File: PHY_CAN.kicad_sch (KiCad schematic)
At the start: 6 parts, among them U3 SN65HVD230, U4 SN65HVD230

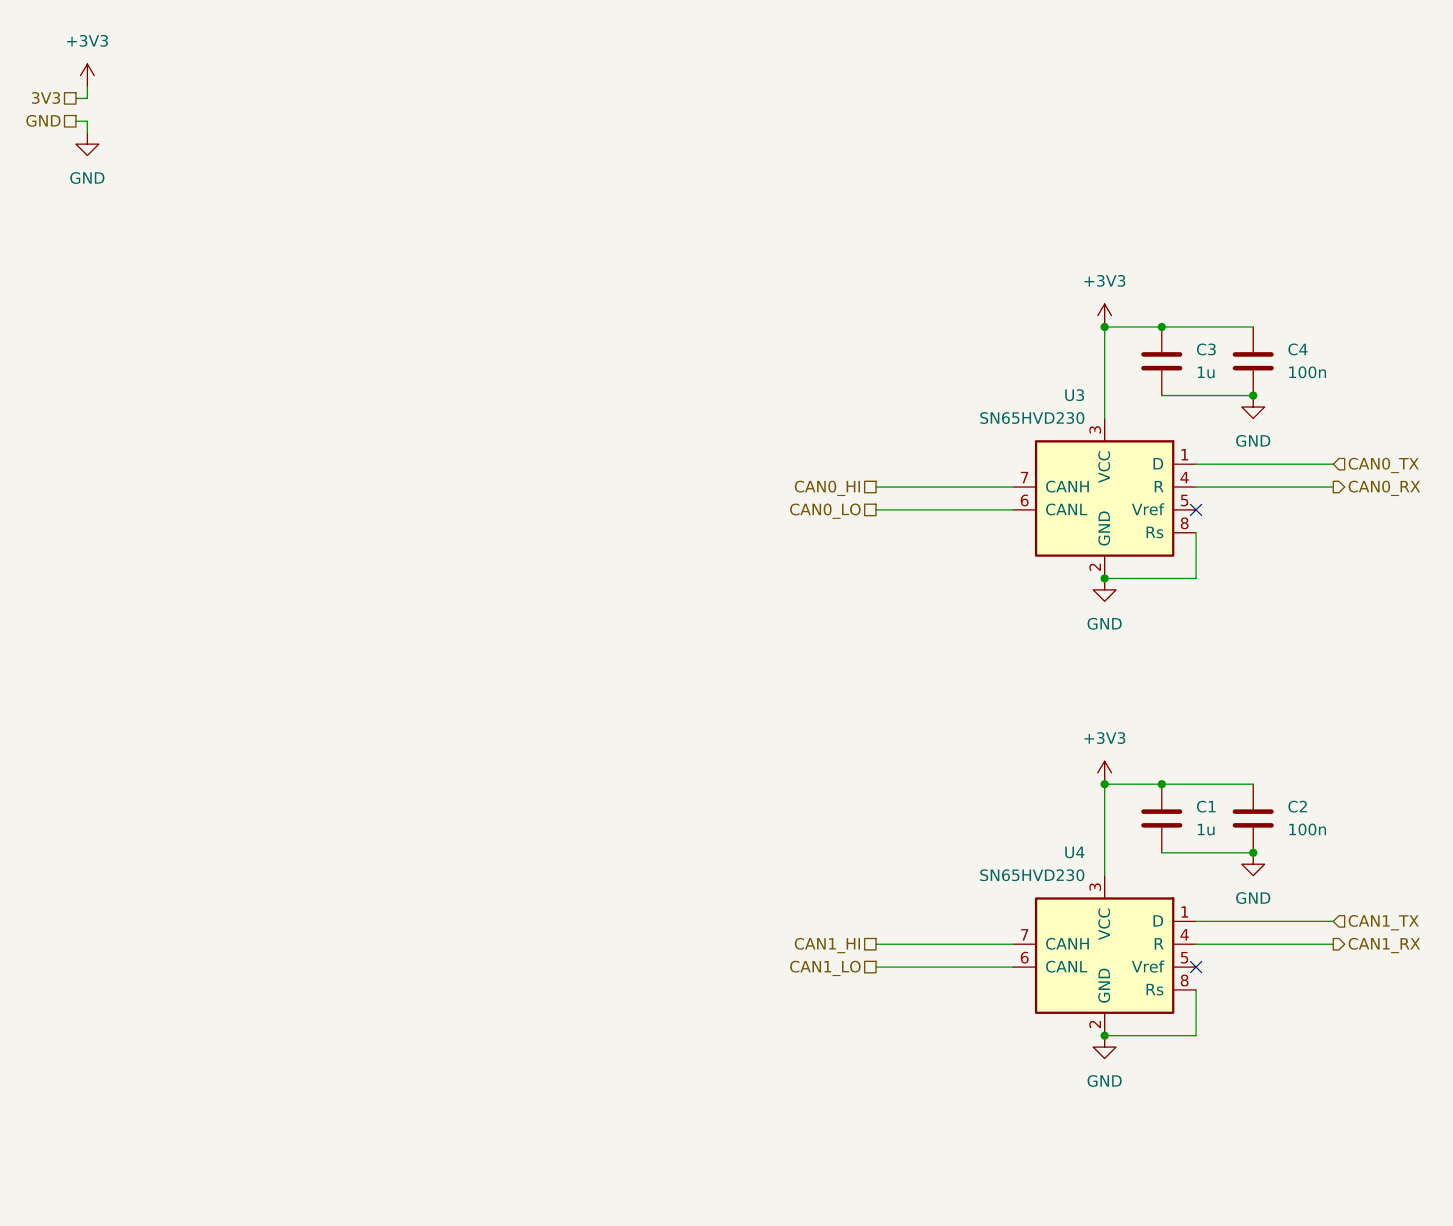
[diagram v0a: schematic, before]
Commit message: routed more sheets, improved analogs. next 5v /analog ground
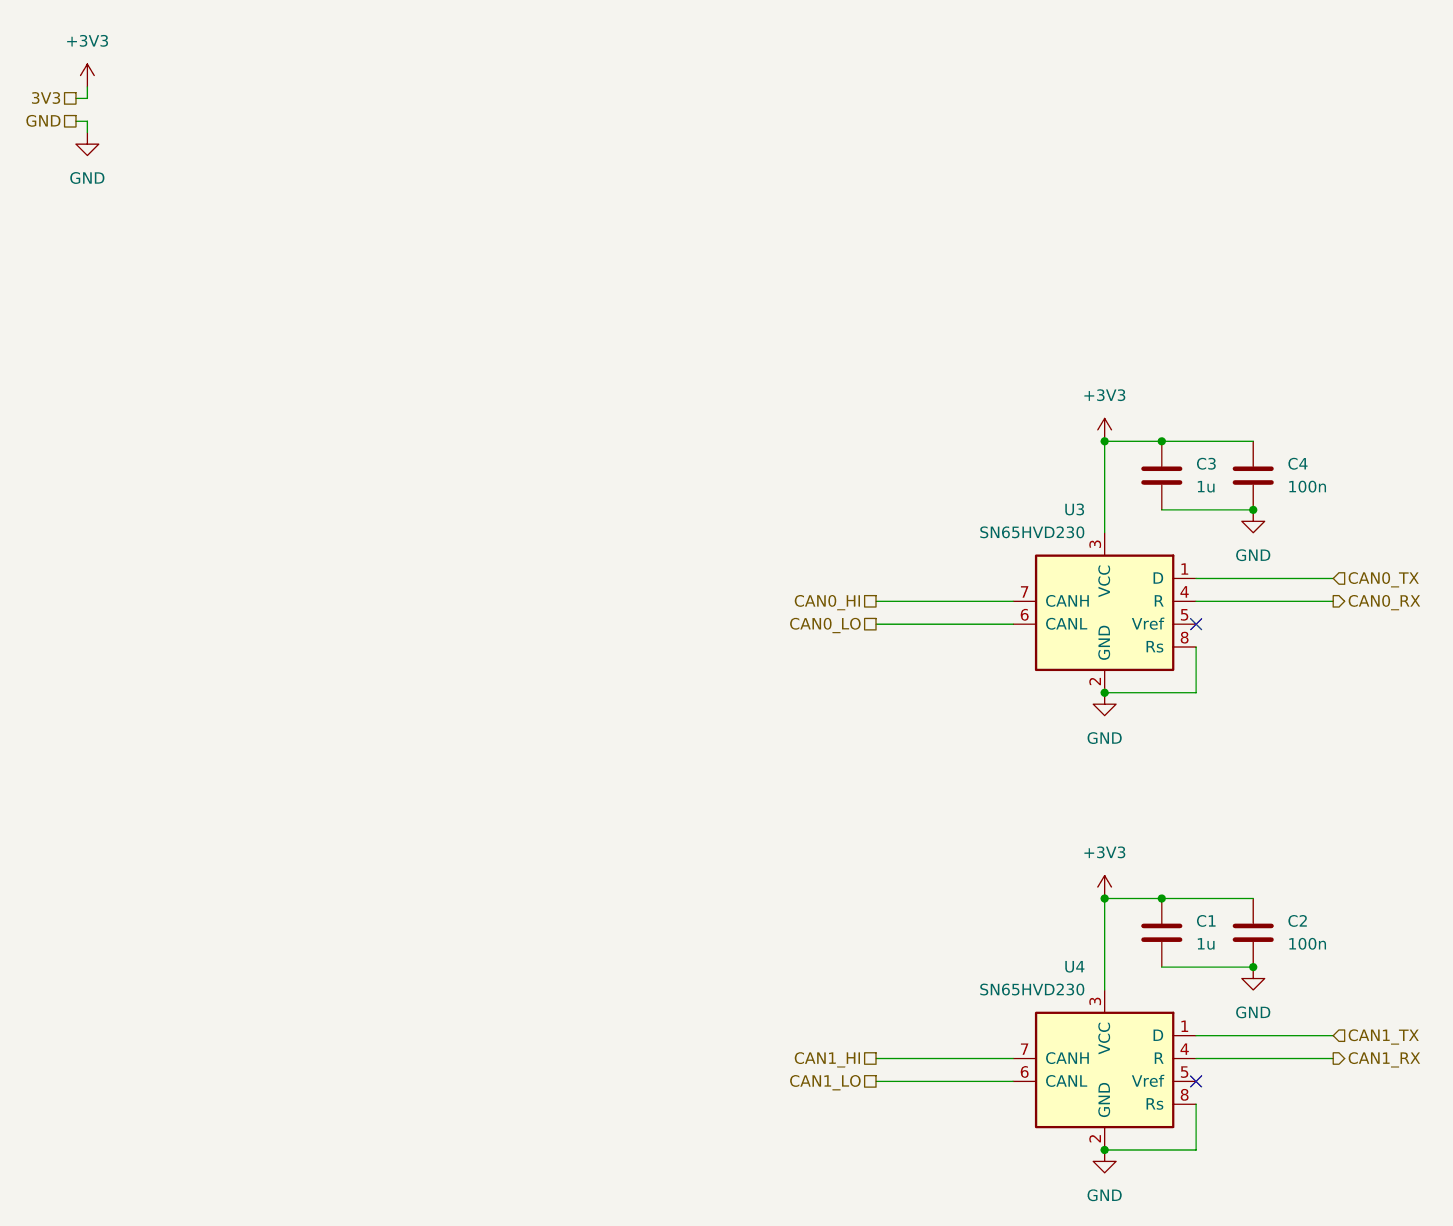
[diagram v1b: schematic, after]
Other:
- moved on the sheet: C1, C2, C3, C4, U3, U4

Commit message: lsd circuit in place
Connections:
- net +3V3 renamed 3V3
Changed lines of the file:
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@@
 			)
 		)
-		(property "Value" "+3V3"
-			(at 26.67 19.05 0)
-			(effects
-				(font
-					(size 1.27 1.27)
-				)
+		(property "Value" "3V3"
+			(at 29.21 22.8599 0)
+			(effects
+				(font
+					(size 1.27 1.27)
+				)
+				(justify left)
 			)
 		)
@@
 			)
 		)
-		(property "Value" "+3V3"
-			(at 139.7 58.42 0)
-			(effects
-				(font
-					(size 1.27 1.27)
-				)
+		(property "Value" "3V3"
+			(at 142.24 62.2299 0)
+			(effects
+				(font
+					(size 1.27 1.27)
+				)
+				(justify left)
 			)
 		)
@@
 			)
 		)
-		(property "Value" "+3V3"
-			(at 139.7 109.22 0)
-			(effects
-				(font
-					(size 1.27 1.27)
-				)
-			)
-		)
+		(property "Value" "3V3"
+			(at 142.24 113.0299 0)
+			(effects
+				(font
+					(size 1.27 1.27)
+				)
+				(justify left)
+			)
+		)

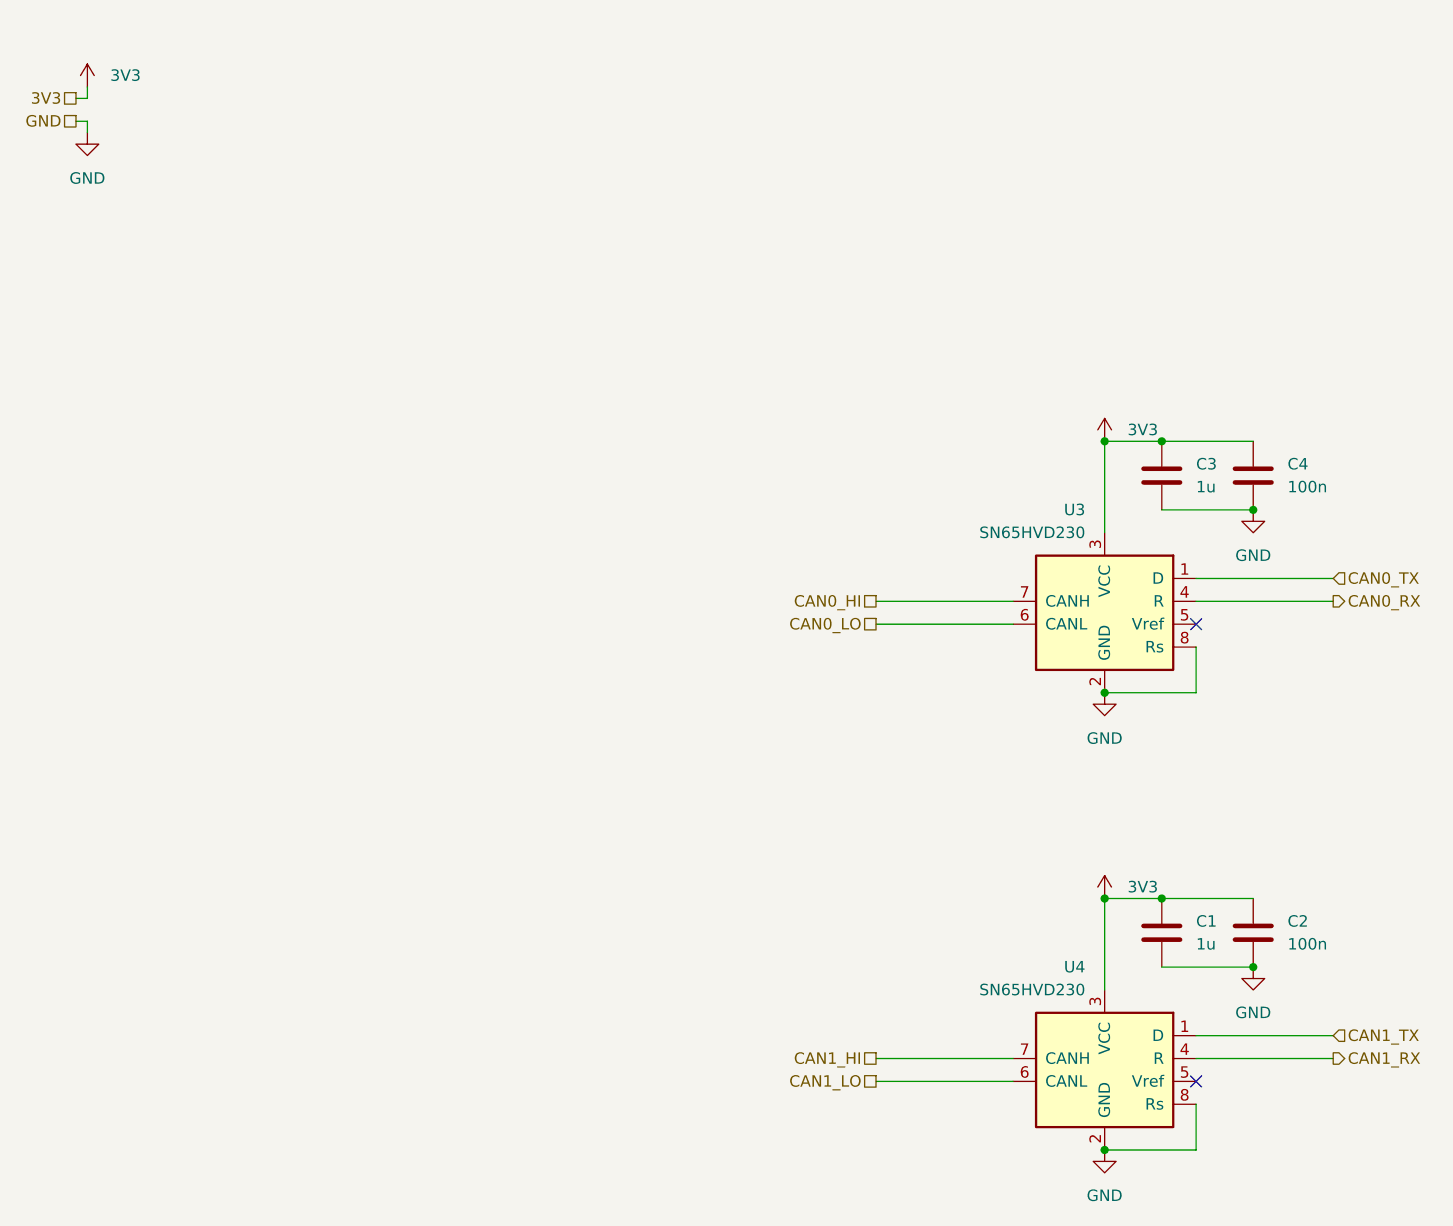
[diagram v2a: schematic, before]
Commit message: added 3.3v gpio input protection
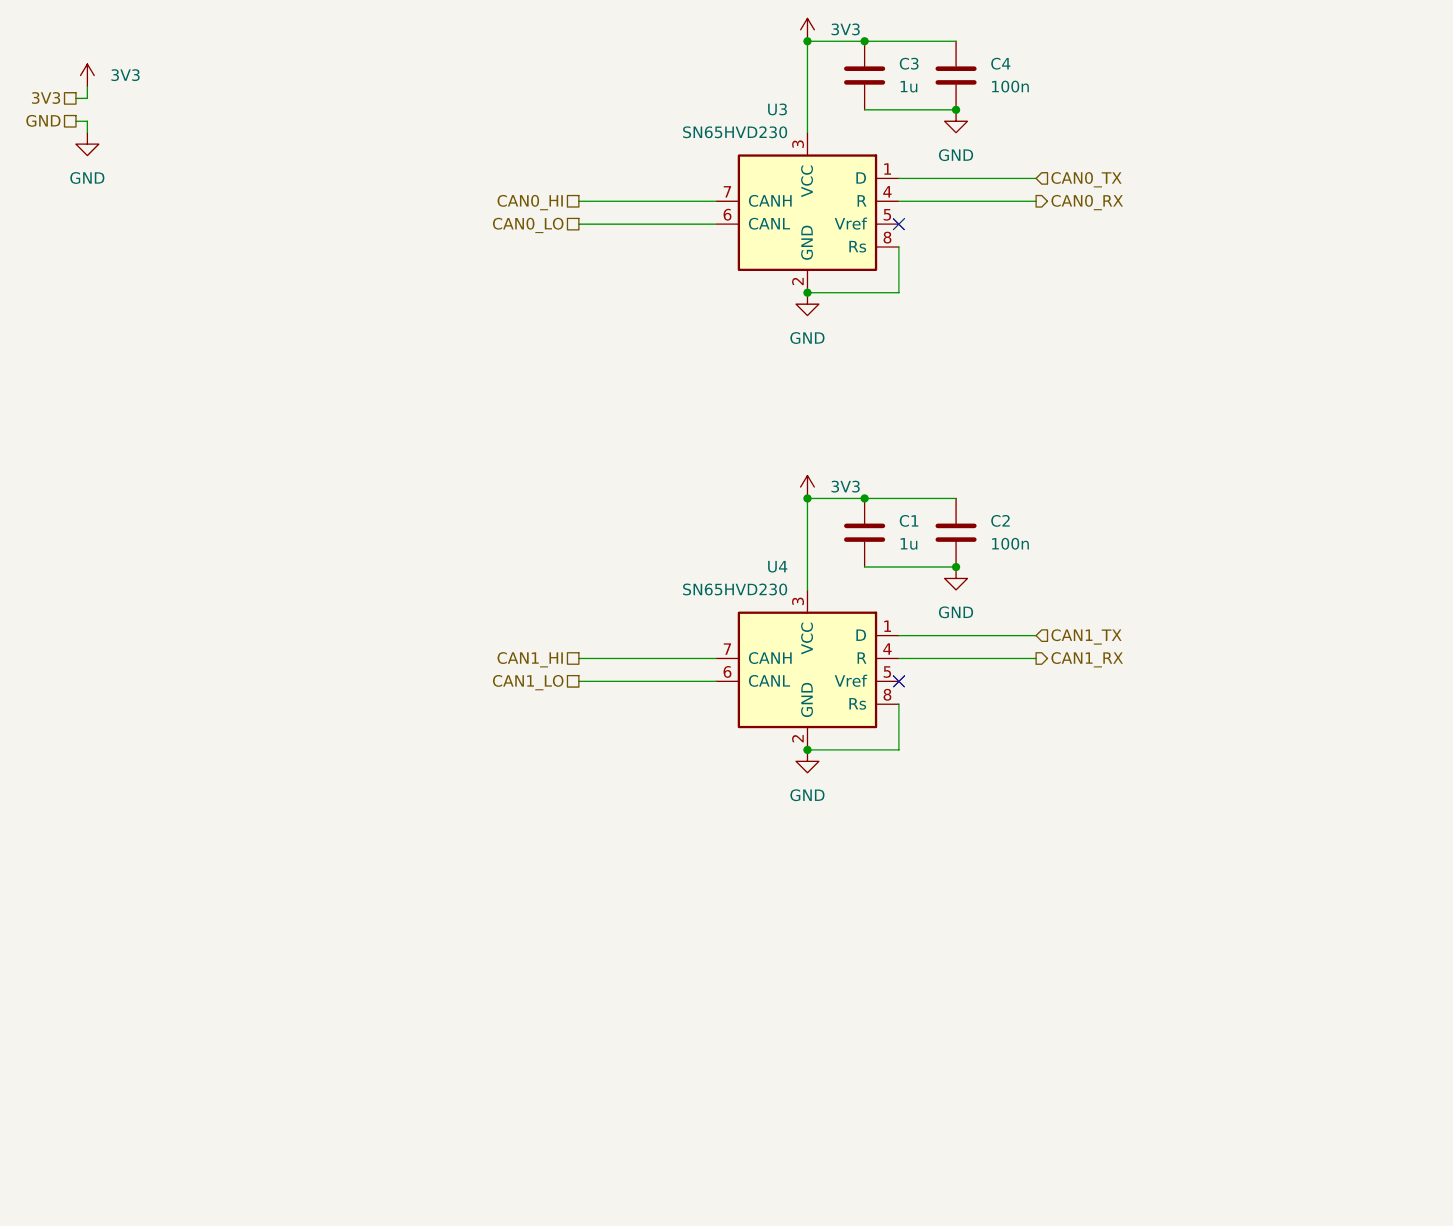
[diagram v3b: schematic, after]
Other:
- moved on the sheet: C1, C2, C3, C4, U3, U4

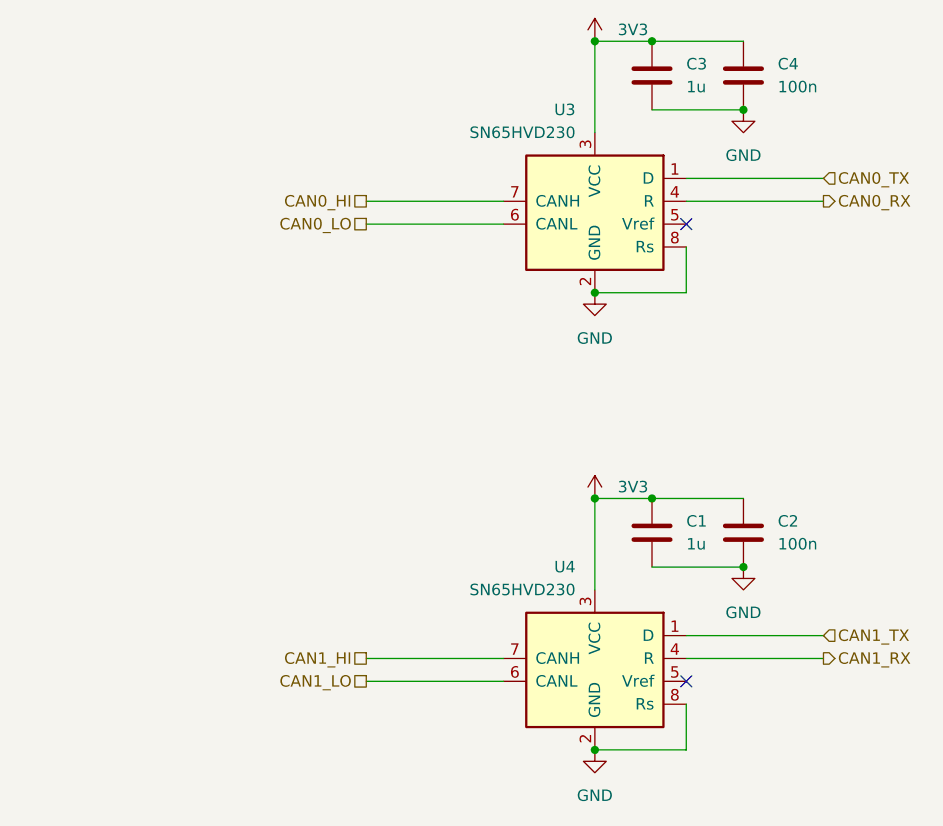
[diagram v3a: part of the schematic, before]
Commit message: updated CAN
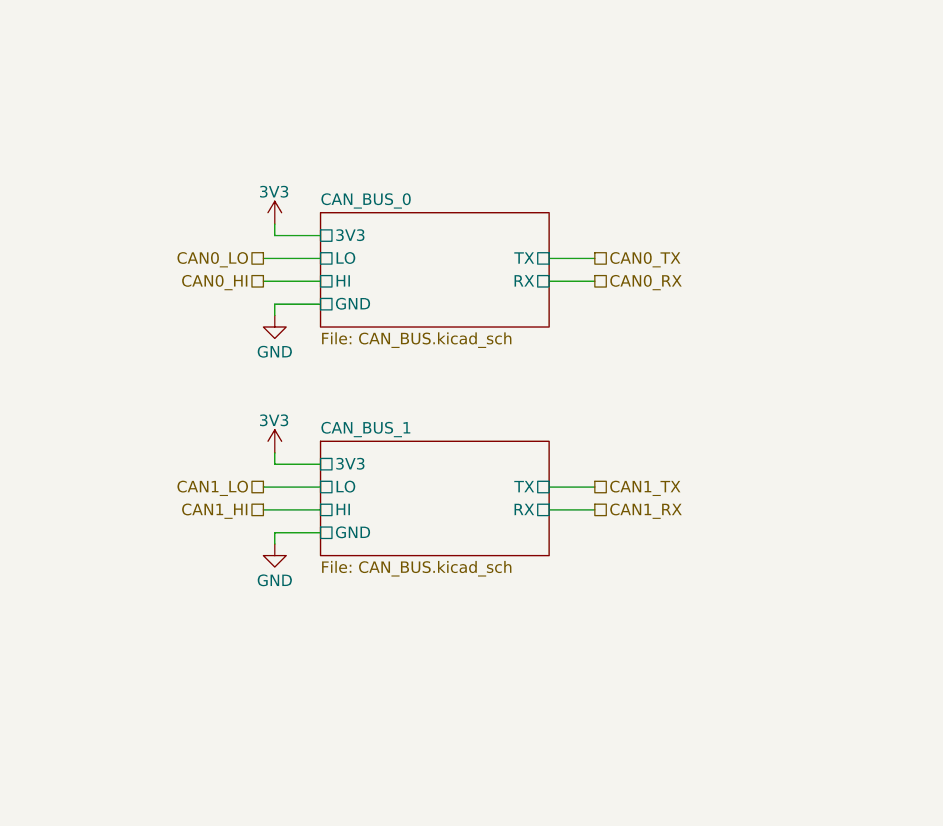
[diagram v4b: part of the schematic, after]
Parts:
- removed C1, C3: 1u, Capacitor_SMD:C_0603_1608Metric, symbol Device:C
- removed C2, C4: 100n, Capacitor_SMD:C_0603_1608Metric, symbol Device:C
- removed U3, U4: SN65HVD230, Package_SO:SOIC-8_3.9x4.9mm_P1.27mm, symbol Interface_CAN_LIN:SN65HVD230
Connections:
- no-connect marks 2 -> 0
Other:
- added sheet CAN_BUS_0 (CAN_BUS.kicad_sch)
- added sheet CAN_BUS_1 (CAN_BUS.kicad_sch)
